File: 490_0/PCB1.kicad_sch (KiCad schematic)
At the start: 3 parts, among them J11 Conn_01x08, J12 0522711579, J13 S2B-ZR

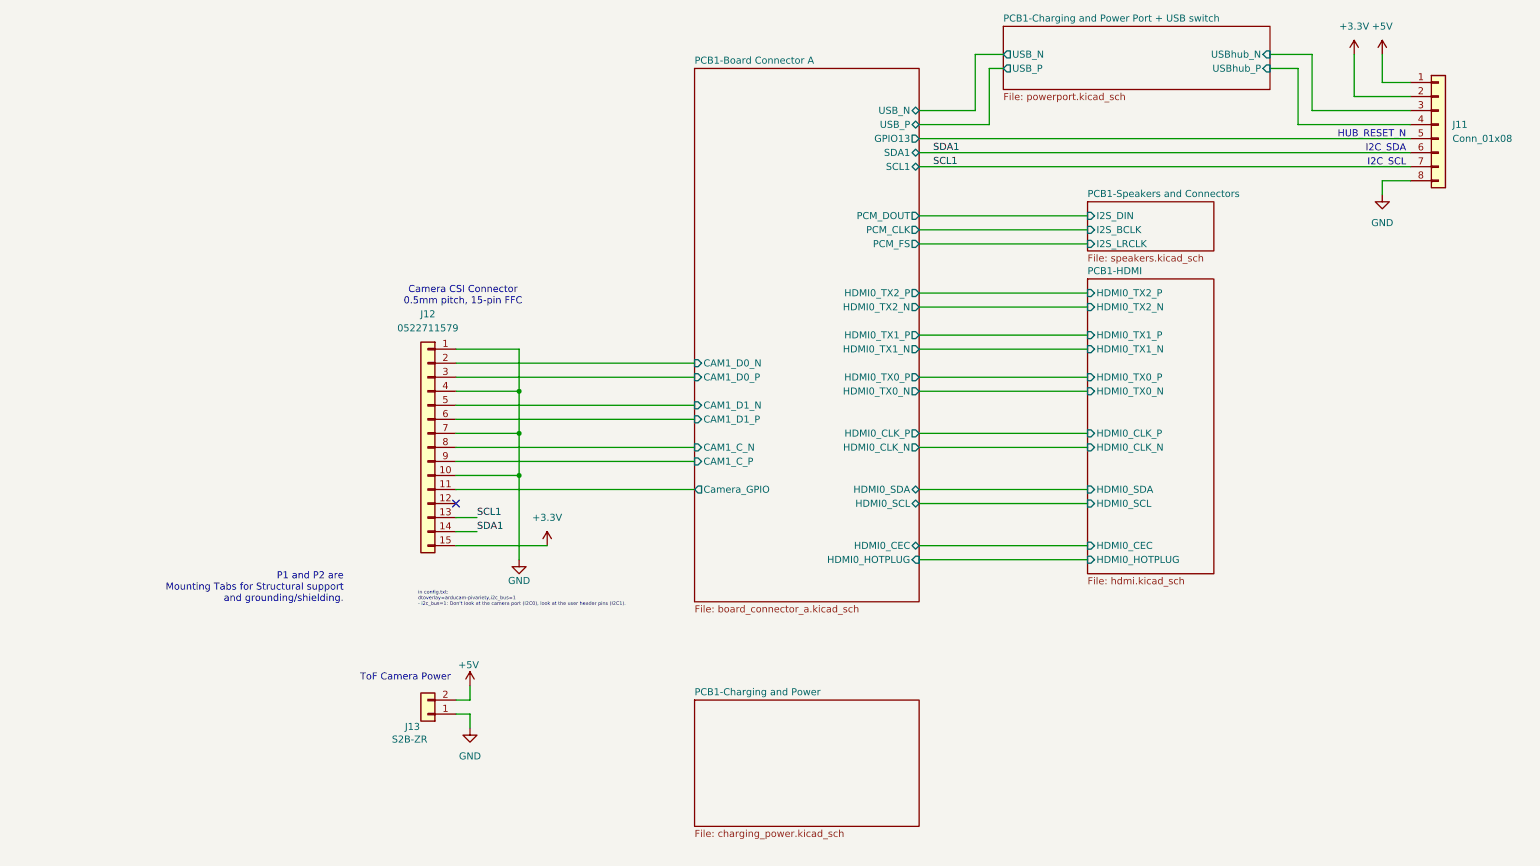
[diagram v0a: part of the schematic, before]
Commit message: FFC to HDMI change
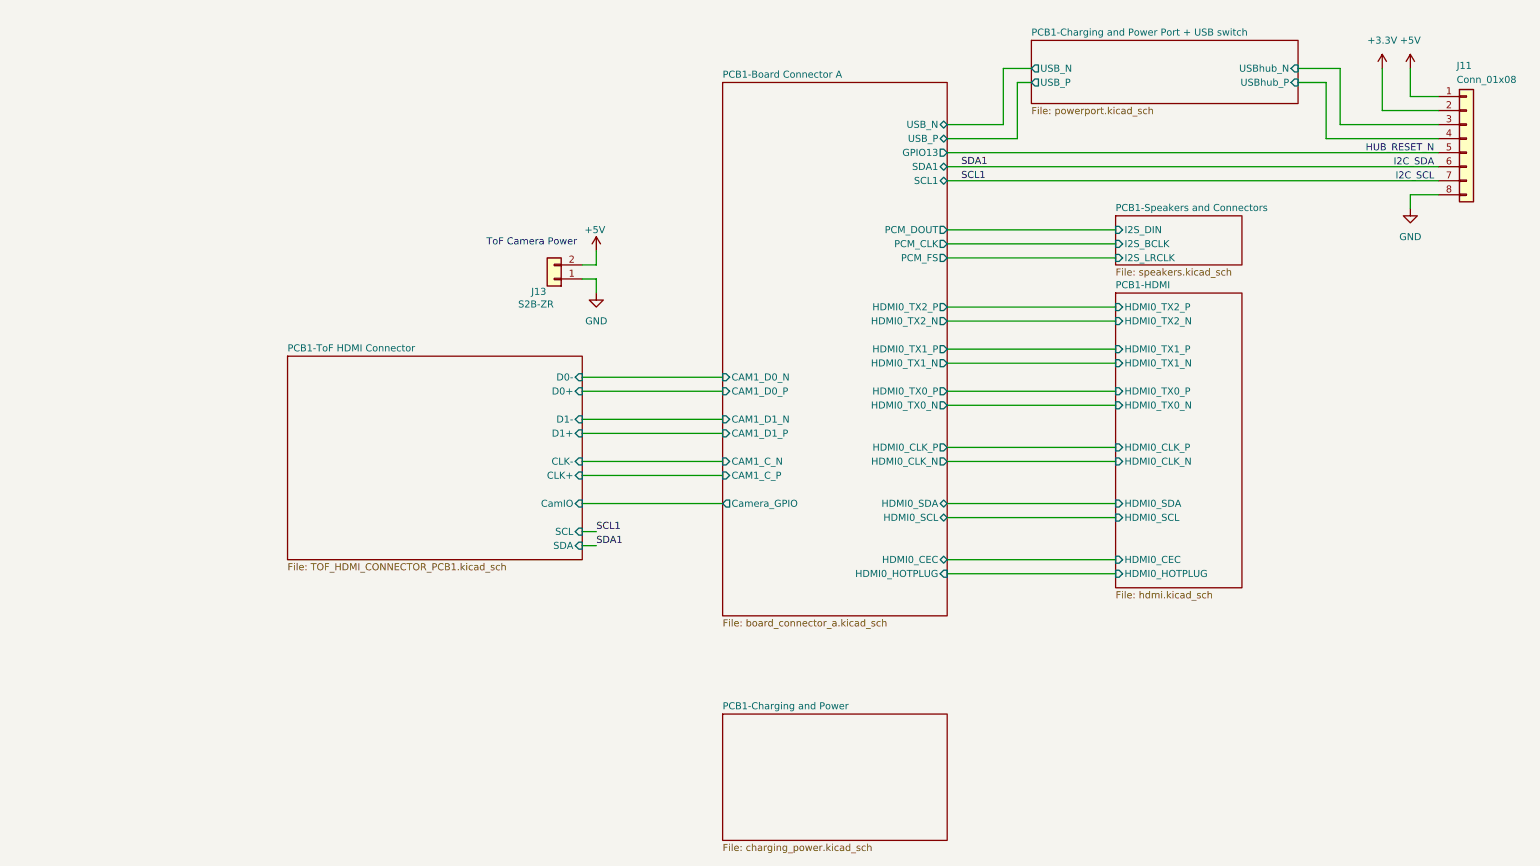
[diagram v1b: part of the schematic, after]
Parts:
- removed J12: 0522711579, symbol Connector_Generic:Conn_01x15
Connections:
- no-connect marks 1 -> 0
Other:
- added sheet PCB1-ToF HDMI Connector (TOF_HDMI_CONNECTOR_PCB1.kicad_sch)
- note removed: "Camera CSI Connector 0.5mm pitch, 15-pin FFC"
- note removed: "P1 and P2 are Mounting Tabs for Structural support and grounding/shielding."
- note removed: "in config.txt: dtoverlay=arducam-pivariety,i2c_bus=1 - i2c_bus=1: Don't look at the camera port (I2C0), look at the user header pins (I2C1)."
- moved on the sheet: J11, J13

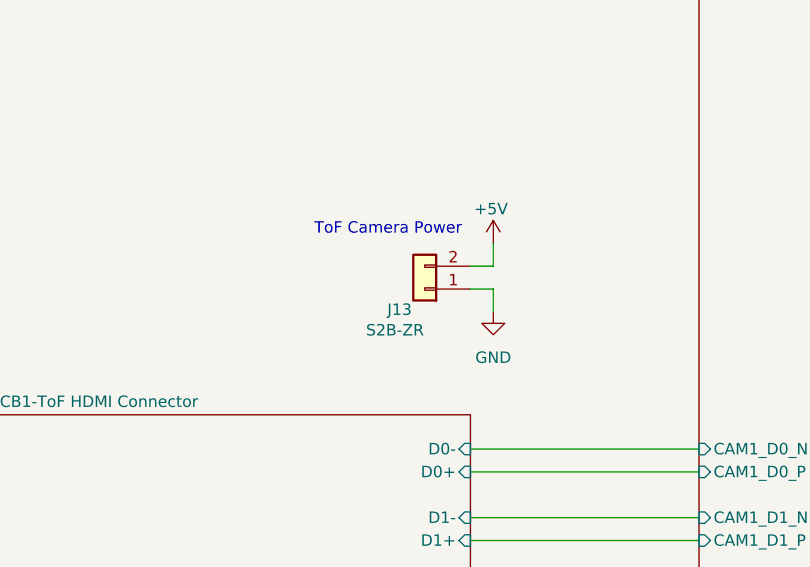
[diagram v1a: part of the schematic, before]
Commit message: ToF power routing
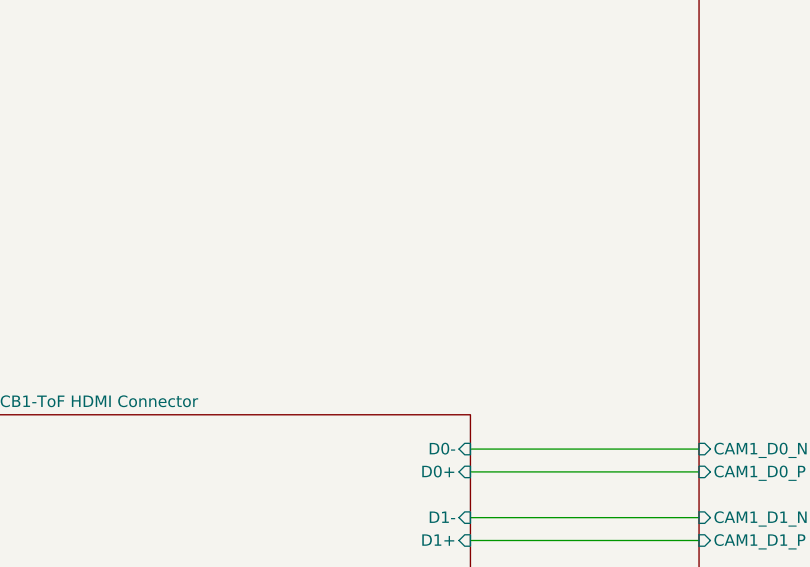
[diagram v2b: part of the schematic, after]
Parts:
- removed J13: S2B-ZR, S2B-XH-A:JST_S2B-XH-A, symbol PCM_4ms_Connector:Conn_01x02
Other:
- note removed: "ToF Camera Power"
